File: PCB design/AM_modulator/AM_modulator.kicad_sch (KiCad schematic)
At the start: 0 parts

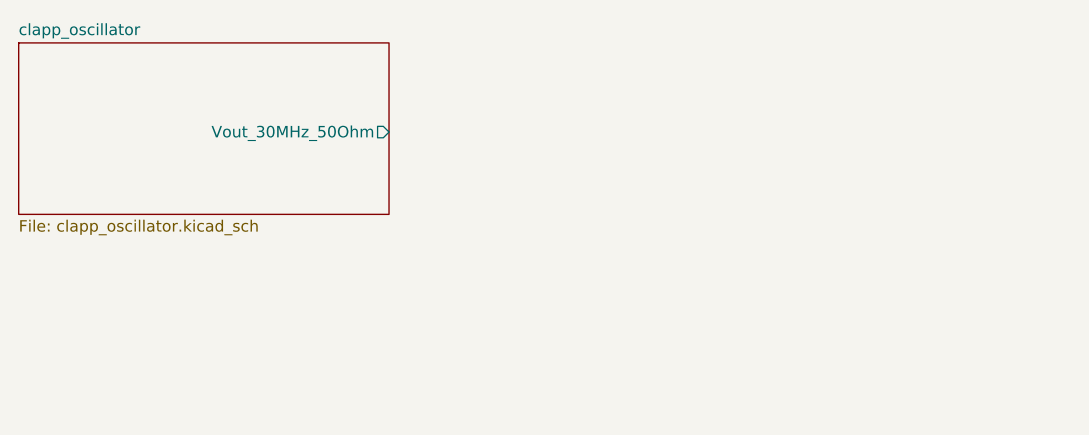
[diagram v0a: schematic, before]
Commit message: Mixer en la placa
Integración del mezclador en la placa
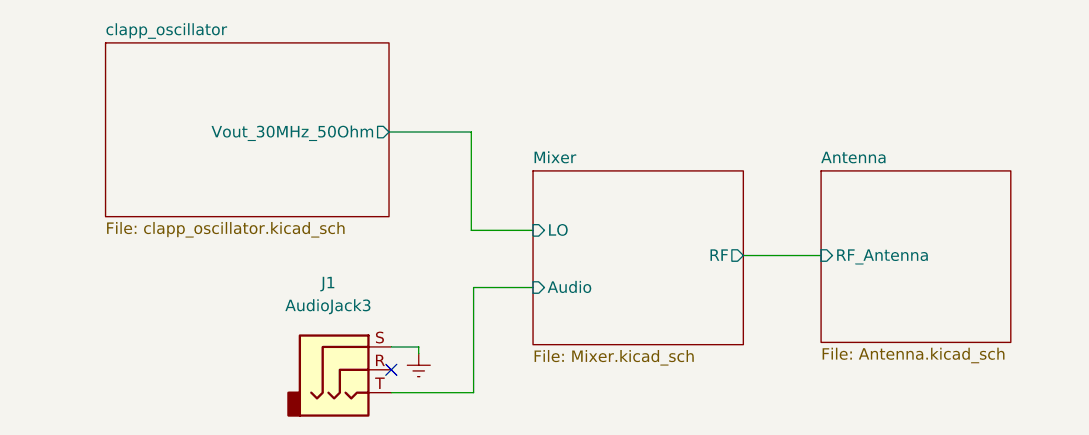
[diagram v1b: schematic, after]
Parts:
- added J1: AudioJack3, Jack Sigma:Jack_Sigma, symbol Connector:AudioJack3
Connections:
- new net Earth: J1.S
- new net Mixer/Audio: J1.T
- no-connect marks 0 -> 1
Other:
- added sheet Antenna (Antenna.kicad_sch)
- added sheet Mixer (Mixer.kicad_sch)

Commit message: Avances placa
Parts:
- added J2: Conn_01x02_Female, Connector_PinSocket_2.54mm:PinSocket_1x02_P2.54mm_Vertical, symbol Connector:Conn_01x02_Female
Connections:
- net Earth renamed GND
- net GND: now also J2.2 (Pin_2)
- new net +12V: J2.1 (Pin_1)
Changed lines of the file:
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@@
+    (stroke (width 0) (type default) (color 0 0 0 0))
+  )
+  (wire (pts (xy 95.504 133.35) (xy 92.964 133.35))
+    (stroke (width 0) (type default) (color 0 0 0 0))
+  )
+  (wire (pts (xy 92.964 133.35) (xy 92.964 134.366))
     (stroke (width 0) (type default) (color 0 0 0 0))
   )
@@
     (stroke (width 0) (type default) (color 0 0 0 0))
   )
+  (wire (pts (xy 92.964 130.81) (xy 95.504 130.81))
+    (stroke (width 0) (type default) (color 0 0 0 0))
+  )
   (wire (pts (xy 99.314 118.872) (xy 108.458 118.872))
     (stroke (width 0) (type default) (color 0 0 0 0))
   )
+  (wire (pts (xy 92.964 129.794) (xy 92.964 130.81))
+    (stroke (width 0) (type default) (color 0 0 0 0))
+  )
   (wire (pts (xy 99.314 113.792) (xy 102.362 113.792))
     (stroke (width 0) (type default) (color 0 0 0 0))
@@
   (wire (pts (xy 138.43 103.632) (xy 147.066 103.632))
     (stroke (width 0) (type default) (color 0 0 0 0))
+  )
+  (symbol (lib_id "Connector:Conn_01x02_Female") (at 100.584 130.81 0) (unit 1)
+    (in_bom yes) (on_board yes) (fields_autoplaced)
+    (property "Reference" "J2" (id 0) (at 102.362 130.8099 0)
+      (effects (font (size 1.27 1.27)) (justify left))
+    )
+    (property "Value" "Conn_01x02_Female" (id 1) (at 102.362 133.3499 0)
+      (effects (font (size 1.27 1.27)) (justify left))
+    )
+    (property "Footprint" "Connector_PinSocket_2.54mm:PinSocket_1x02_P2.54mm_Vertical" (id 2) (at 100.584 130.81 0)
+      (effects (font (size 1.27 1.27)) hide)
+    )
+    (property "Datasheet" "~" (id 3) (at 100.584 130.81 0)
+      (effects (font (size 1.27 1.27)) hide)
+    )
+    (pin "1")
+    (pin "2")
+  )
+  (symbol (lib_id "power:GND") (at 92.964 134.366 0) (unit 1)
+    (in_bom yes) (on_board yes) (fields_autoplaced)
+    (property "Reference" "#PWR0115" (id 0) (at 92.964 140.716 0)
+      (effects (font (size 1.27 1.27)) hide)
+    )
+    (property "Value" "GND" (id 1) (at 92.964 139.7 0))
+    (property "Footprint" "" (id 2) (at 92.964 134.366 0)
+      (effects (font (size 1.27 1.27)) hide)
+    )
+    (property "Datasheet" "" (id 3) (at 92.964 134.366 0)
+      (effects (font (size 1.27 1.27)) hide)
+    )
+    (pin "1")
+  )
+  (symbol (lib_id "power:GND") (at 102.362 114.554 0) (unit 1)
+    (in_bom yes) (on_board yes)
+    (property "Reference" "#PWR0104" (id 0) (at 102.362 120.904 0)
+      (effects (font (size 1.27 1.27)) hide)
+    )
+    (property "Value" "GND" (id 1) (at 105.156 116.84 0))
+    (property "Footprint" "" (id 2) (at 102.362 114.554 0)
+      (effects (font (size 1.27 1.27)) hide)
+    )
+    (property "Datasheet" "" (id 3) (at 102.362 114.554 0)
+      (effects (font (size 1.27 1.27)) hide)
+    )
+    (pin "1")
   )
   (symbol (lib_id "Connector:AudioJack3") (at 94.234 116.332 0) (unit 1)
@@
     (pin "T")
   )
-  (symbol (lib_id "power:Earth") (at 102.362 114.554 0) (unit 1)
-    (in_bom yes) (on_board yes) (fields_autoplaced)
-    (property "Reference" "#PWR0104" (id 0) (at 102.362 120.904 0)
-      (effects (font (size 1.27 1.27)) hide)
-    )
-    (property "Value" "Earth" (id 1) (at 102.362 118.364 0)
-      (effects (font (size 1.27 1.27)) hide)
-    )
-    (property "Footprint" "" (id 2) (at 102.362 114.554 0)
-      (effects (font (size 1.27 1.27)) hide)
-    )
-    (property "Datasheet" "~" (id 3) (at 102.362 114.554 0)
+  (symbol (lib_id "power:+12V") (at 92.964 129.794 0) (unit 1)
+    (in_bom yes) (on_board yes) (fields_autoplaced)
+    (property "Reference" "#PWR0114" (id 0) (at 92.964 133.604 0)
+      (effects (font (size 1.27 1.27)) hide)
+    )
+    (property "Value" "+12V" (id 1) (at 92.964 124.206 0))
+    (property "Footprint" "" (id 2) (at 92.964 129.794 0)
+      (effects (font (size 1.27 1.27)) hide)
+    )
+    (property "Datasheet" "" (id 3) (at 92.964 129.794 0)
       (effects (font (size 1.27 1.27)) hide)
     )
@@
       (reference "#PWR0103") (unit 1) (value "GND") (footprint "")
     )
-    (path "/e72d0ece-779f-4775-826c-9e9158d688b7"
-      (reference "#PWR0104") (unit 1) (value "Earth") (footprint "")
+    (path "/427fcc87-3472-4a51-a31e-5e28ee0d1d77"
+      (reference "#PWR0104") (unit 1) (value "GND") (footprint "")
     )
     (path "/feaeab96-fb10-4d9a-9465-54f6467279a4/1e2a57ec-1382-46c3-aa4f-2c20399f7e14"
@@
       (reference "#PWR0113") (unit 1) (value "GND") (footprint "")
     )
+    (path "/b8fa672a-7e3f-4440-b60f-8138c3aa3d79"
+      (reference "#PWR0114") (unit 1) (value "+12V") (footprint "")
+    )
+    (path "/1d1a2ac1-d40d-4ac1-b9da-c646f87723af"
+      (reference "#PWR0115") (unit 1) (value "GND") (footprint "")
+    )
+    (path "/e320c07d-9db6-4a2f-b06e-cc71a93af112/1a997f66-1479-44f7-9ecd-d894e641c671"
+      (reference "#PWR?") (unit 1) (value "GND") (footprint "")
+    )
+    (path "/e320c07d-9db6-4a2f-b06e-cc71a93af112/3f026fc4-4226-4af0-b36b-a8d4d6de9b4e"
+      (reference "Antena+1") (unit 1) (value "Conn_01x01_Female") (footprint "Connector_Pin:Pin_D1.4mm_L8.5mm_W2.8mm_FlatFork")
+    )
+    (path "/e320c07d-9db6-4a2f-b06e-cc71a93af112/086129ee-0e83-4411-a999-f62e821a923a"
+      (reference "Antena-1") (unit 1) (value "Conn_01x01_Female") (footprint "Connector_Pin:Pin_D1.4mm_L8.5mm_W2.8mm_FlatFork")
+    )
     (path "/feaeab96-fb10-4d9a-9465-54f6467279a4/49010381-7b9d-48b7-bf68-c72f022c5a30"
       (reference "C1") (unit 1) (value "1n") (footprint "Capacitor_SMD:C_0805_2012Metric_Pad1.18x1.45mm_HandSolder")
@@
       (reference "CMa1") (unit 1) (value "100n") (footprint "Capacitor_SMD:C_0805_2012Metric_Pad1.18x1.45mm_HandSolder")
     )
-    (path "/d4b71b3f-86db-4677-a185-1a235c83ef21/e3d26ab9-e477-4e84-9c6e-5c64263b5b2d"
-      (reference "CMan1") (unit 1) (value "33p") (footprint "Capacitor_SMD:C_0805_2012Metric_Pad1.18x1.45mm_HandSolder")
-    )
     (path "/e320c07d-9db6-4a2f-b06e-cc71a93af112/61e2669f-d348-4de3-a399-01927efd15f2"
       (reference "Cpi1") (unit 1) (value "C") (footprint "Capacitor_SMD:C_0805_2012Metric_Pad1.18x1.45mm_HandSolder")
@@
       (reference "Cpi2") (unit 1) (value "C") (footprint "Capacitor_SMD:C_0805_2012Metric_Pad1.18x1.45mm_HandSolder")
     )
+    (path "/e320c07d-9db6-4a2f-b06e-cc71a93af112/4fc9bb7f-d4c2-4bbb-8850-dce57ee165d3"
+      (reference "Cpi11") (unit 1) (value "C") (footprint "Capacitor_SMD:C_0805_2012Metric_Pad1.18x1.45mm_HandSolder")
+    )
+    (path "/e320c07d-9db6-4a2f-b06e-cc71a93af112/f3f7a540-3942-42f8-b970-f07a5c077913"
+      (reference "Cpi21") (unit 1) (value "C") (footprint "Capacitor_SMD:C_0805_2012Metric_Pad1.18x1.45mm_HandSolder")
+    )
     (path "/feaeab96-fb10-4d9a-9465-54f6467279a4/e1e15d2e-1fcb-496b-9f63-7fd690ae5b87"
       (reference "Cv1") (unit 1) (value "30p") (footprint "capacitors:variable_cap")
@@
       (reference "J1") (unit 1) (value "AudioJack3") (footprint "Jack Sigma:Jack_Sigma")
     )
-    (path "/e320c07d-9db6-4a2f-b06e-cc71a93af112/97fb4d0f-b247-407f-b8a6-832f9683ebd9"
+    (path "/0a2b3a26-011b-46b9-85a0-5a78834b9695"
       (reference "J2") (unit 1) (value "Conn_01x02_Female") (footprint "Connector_PinSocket_2.54mm:PinSocket_1x02_P2.54mm_Vertical")
     )
@@
     )
     (path "/e320c07d-9db6-4a2f-b06e-cc71a93af112/37e4f729-c5d0-4d27-b6f5-32a39cbcbef0"
-      (reference "Lpi1") (unit 1) (value "L") (footprint "")
+      (reference "Lpi1") (unit 1) (value "L") (footprint "Inductor_THT:L_Toroid_Vertical_L21.6mm_W9.1mm_P8.40mm_Bourns_5700")
     )
     (path "/feaeab96-fb10-4d9a-9465-54f6467279a4/9e03f67f-c2c7-4258-b034-512fafb9869e"
@@
     )
     (path "/d4b71b3f-86db-4677-a185-1a235c83ef21/fc643576-5c36-45b1-a67c-10c88ca1a82f"
-      (reference "RMc") (unit 1) (value "220") (footprint "Resistor_SMD:R_0805_2012Metric_Pad1.20x1.40mm_HandSolder")
+      (reference "RMc1") (unit 1) (value "220") (footprint "Resistor_SMD:R_0805_2012Metric_Pad1.20x1.40mm_HandSolder")
     )
     (path "/d4b71b3f-86db-4677-a185-1a235c83ef21/5a93effd-0e24-4bec-86ea-df638bde0dae"

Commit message: PCB 2.0
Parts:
- added SW1, SW2: SW_DIP_x01, Resistor_SMD:R_0603_1608Metric_Pad0.98x0.95mm_HandSolder, symbol Switch:SW_DIP_x01
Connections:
- net Antenna/RF_Antenna: now also SW2.2
- net Mixer/LO: now also SW1.2
- new net Mixer/RF: SW2.1
- new net clapp_oscillator/Vout_30MHz_50Ohm: SW1.1
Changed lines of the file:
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@@
     (stroke (width 0) (type default) (color 0 0 0 0))
   )
-  (wire (pts (xy 99.06 89.916) (xy 108.204 89.916))
-    (stroke (width 0) (type default) (color 0 0 0 0))
-  )
-  (wire (pts (xy 108.204 89.916) (xy 108.204 100.838))
+  (wire (pts (xy 64.516 100.838) (xy 77.978 100.838))
     (stroke (width 0) (type default) (color 0 0 0 0))
   )
@@
     (stroke (width 0) (type default) (color 0 0 0 0))
   )
+  (wire (pts (xy 93.218 100.838) (xy 115.062 100.838))
+    (stroke (width 0) (type default) (color 0 0 0 0))
+  )
   (wire (pts (xy 99.314 113.792) (xy 102.362 113.792))
     (stroke (width 0) (type default) (color 0 0 0 0))
   )
-  (wire (pts (xy 108.204 100.838) (xy 115.062 100.838))
-    (stroke (width 0) (type default) (color 0 0 0 0))
-  )
-  (wire (pts (xy 138.43 103.632) (xy 147.066 103.632))
+  (wire (pts (xy 163.322 103.632) (xy 177.292 103.632))
+    (stroke (width 0) (type default) (color 0 0 0 0))
+  )
+  (wire (pts (xy 138.43 103.632) (xy 148.082 103.632))
     (stroke (width 0) (type default) (color 0 0 0 0))
   )
@@
     (pin "1")
   )
+  (symbol (lib_id "Switch:SW_DIP_x01") (at 85.598 100.838 0) (unit 1)
+    (in_bom yes) (on_board yes) (fields_autoplaced)
+    (property "Reference" "SW1" (id 0) (at 85.598 92.456 0))
+    (property "Value" "SW_DIP_x01" (id 1) (at 85.598 94.996 0))
+    (property "Footprint" "Resistor_SMD:R_0603_1608Metric_Pad0.98x0.95mm_HandSolder" (id 2) (at 85.598 100.838 0)
+      (effects (font (size 1.27 1.27)) hide)
+    )
+    (property "Datasheet" "~" (id 3) (at 85.598 100.838 0)
+      (effects (font (size 1.27 1.27)) hide)
+    )
+    (pin "1")
+    (pin "2")
+  )
   (symbol (lib_id "Connector:AudioJack3") (at 94.234 116.332 0) (unit 1)
     (in_bom yes) (on_board yes) (fields_autoplaced)
@@
     (pin "S")
     (pin "T")
+  )
+  (symbol (lib_id "Switch:SW_DIP_x01") (at 155.702 103.632 0) (unit 1)
+    (in_bom yes) (on_board yes) (fields_autoplaced)
+    (property "Reference" "SW2" (id 0) (at 155.702 95.25 0))
+    (property "Value" "SW_DIP_x01" (id 1) (at 155.702 97.79 0))
+    (property "Footprint" "Resistor_SMD:R_0603_1608Metric_Pad0.98x0.95mm_HandSolder" (id 2) (at 155.702 103.632 0)
+      (effects (font (size 1.27 1.27)) hide)
+    )
+    (property "Datasheet" "~" (id 3) (at 155.702 103.632 0)
+      (effects (font (size 1.27 1.27)) hide)
+    )
+    (pin "1")
+    (pin "2")
   )
   (symbol (lib_id "power:+12V") (at 92.964 129.794 0) (unit 1)
@@
     )
   )
-  (sheet (at 147.066 94.234) (size 21.082 19.05) (fields_autoplaced)
+  (sheet (at 177.292 94.234) (size 21.082 19.05) (fields_autoplaced)
     (stroke (width 0.1524) (type solid) (color 0 0 0 0))
     (fill (color 0 0 0 0.0000))
-    (property "Sheet name" "Antenna" (id 0) (at 147.066 93.5224 0)
+    (property "Sheet name" "Antenna" (id 0) (at 177.292 93.5224 0)
       (effects (font (size 1.27 1.27)) (justify left bottom))
     )
-    (property "Sheet file" "Antenna.kicad_sch" (id 1) (at 147.066 113.8686 0)
+    (property "Sheet file" "Antenna.kicad_sch" (id 1) (at 177.292 113.8686 0)
       (effects (font (size 1.27 1.27)) (justify left top))
     )
-    (pin "RF_Antenna" input (at 147.066 103.632 180)
-      (effects (font (size 1.27 1.27)) (justify left))
-    )
-  )
-  (sheet (at 67.564 80.01) (size 31.496 19.304) (fields_autoplaced)
+    (pin "RF_Antenna" input (at 177.292 103.632 180)
+      (effects (font (size 1.27 1.27)) (justify left))
+    )
+  )
+  (sheet (at 33.02 90.932) (size 31.496 19.304) (fields_autoplaced)
     (stroke (width 0.1524) (type solid) (color 0 0 0 0))
     (fill (color 0 0 0 0.0000))
-    (property "Sheet name" "clapp_oscillator" (id 0) (at 67.564 79.2984 0)
+    (property "Sheet name" "clapp_oscillator" (id 0) (at 33.02 90.2204 0)
       (effects (font (size 1.27 1.27)) (justify left bottom))
     )
-    (property "Sheet file" "clapp_oscillator.kicad_sch" (id 1) (at 67.564 99.8986 0)
+    (property "Sheet file" "clapp_oscillator.kicad_sch" (id 1) (at 33.02 110.8206 0)
       (effects (font (size 1.27 1.27)) (justify left top))
     )
-    (pin "Vout_30MHz_50Ohm" output (at 99.06 89.916 0)
+    (pin "Vout_30MHz_50Ohm" output (at 64.516 100.838 0)
       (effects (font (size 1.27 1.27)) (justify right))
     )
@@
       (reference "J2") (unit 1) (value "Conn_01x02_Female") (footprint "Connector_PinSocket_2.54mm:PinSocket_1x02_P2.54mm_Vertical")
     )
+    (path "/feaeab96-fb10-4d9a-9465-54f6467279a4/8f9c2a0c-4f24-4d7d-b742-934174e3493b"
+      (reference "J3") (unit 1) (value "SMA_CONNECTOR") (footprint "SMA_T:LPRS_SMA_CONNECTOR")
+    )
     (path "/d4b71b3f-86db-4677-a185-1a235c83ef21/38c035e7-c5aa-4f04-a554-7240daa9d307"
-      (reference "J?") (unit 1) (value "SMA_CONNECTOR") (footprint "LPRS_SMA_CONNECTOR")
-    )
-    (path "/feaeab96-fb10-4d9a-9465-54f6467279a4/8f9c2a0c-4f24-4d7d-b742-934174e3493b"
-      (reference "J?") (unit 1) (value "SMA_CONNECTOR") (footprint "LPRS_SMA_CONNECTOR")
+      (reference "J4") (unit 1) (value "SMA_CONNECTOR") (footprint "SMA_T:LPRS_SMA_CONNECTOR")
     )
     (path "/feaeab96-fb10-4d9a-9465-54f6467279a4/d2c12894-e46a-4333-bc72-5a352c43c894"
@@
       (reference "RMe1") (unit 1) (value "100") (footprint "Resistor_SMD:R_1206_3216Metric_Pad1.30x1.75mm_HandSolder")
     )
-  )
+    (path "/4b4c1620-39b7-48db-b3d9-b6116428ba55"
+      (reference "SW1") (unit 1) (value "SW_DIP_x01") (footprint "Resistor_SMD:R_0603_1608Metric_Pad0.98x0.95mm_HandSolder")
+    )
+    (path "/76fc3219-24fa-40c8-afc6-9c4c22ce1e83"
+      (reference "SW2") (unit 1) (value "SW_DIP_x01") (footprint "Resistor_SMD:R_0603_1608Metric_Pad0.98x0.95mm_HandSolder")
+    )
+    (path "/feaeab96-fb10-4d9a-9465-54f6467279a4/0c39cb30-aae3-4da0-9aef-dd6049463103"
+      (reference "SW3") (unit 1) (value "SW_DIP_x01") (footprint "Resistor_SMD:R_0603_1608Metric_Pad0.98x0.95mm_HandSolder")
+    )
+    (path "/d4b71b3f-86db-4677-a185-1a235c83ef21/32f46ed6-c307-4e65-bb89-b4a86e21d73b"
+      (reference "SW4") (unit 1) (value "SW_DIP_x01") (footprint "Resistor_SMD:R_0603_1608Metric_Pad0.98x0.95mm_HandSolder")
+    )
+  )

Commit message: PCB design done
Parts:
- removed SW1, SW2: SW_DIP_x01, Resistor_SMD:R_0603_1608Metric_Pad0.98x0.95mm_HandSolder, symbol Switch:SW_DIP_x01
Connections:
- net Mixer/Audio renamed audio
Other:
- added sheet SMA_probe (SMA_probe.kicad_sch)
- added sheet SMA_probe1 (SMA_probe.kicad_sch)
- sheet Mixer ports: added msg; removed Audio
- moved on the sheet: J1, J2
